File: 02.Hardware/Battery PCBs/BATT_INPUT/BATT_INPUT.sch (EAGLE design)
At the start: 39 parts, among them J1 70AAJ-4-M0, J4 DX07S016JA1R1500, U1 AT24C16D-STUM-T, U5 BQ24075, U9 Value

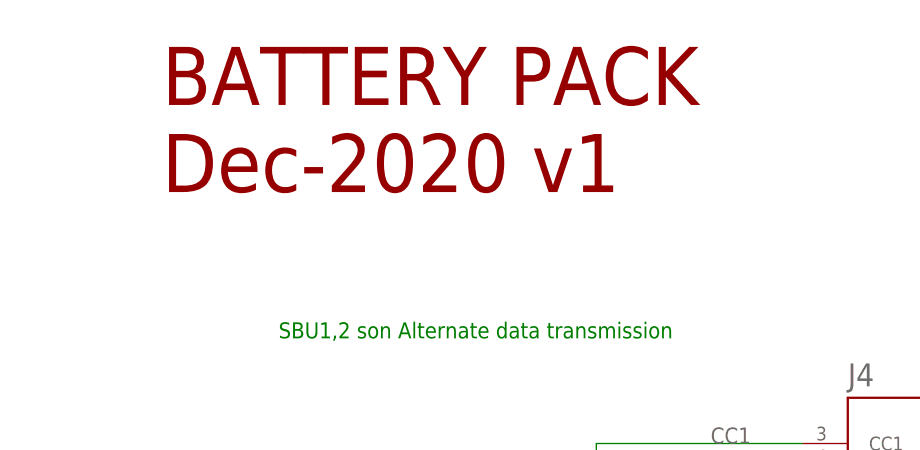
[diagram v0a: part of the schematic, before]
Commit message: Reorganizacion de directorios
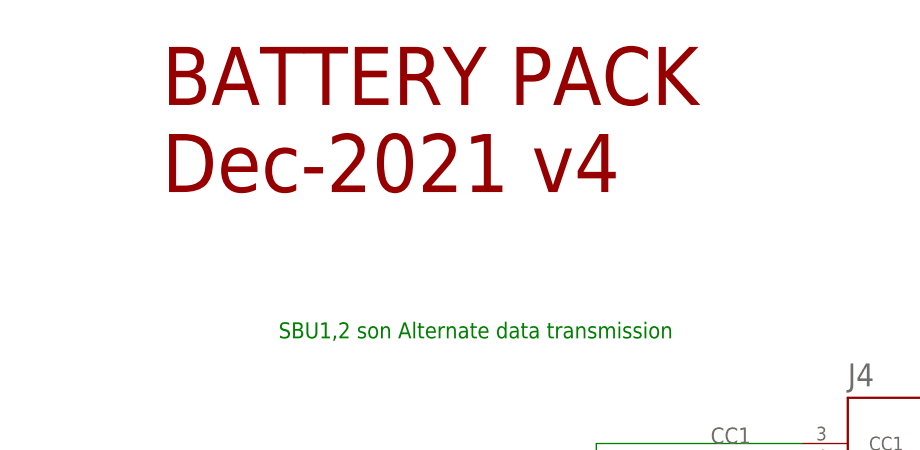
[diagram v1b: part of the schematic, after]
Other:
- note added: "BATTERY PACK Dec-2021 v4"
- note removed: "BATTERY PACK Dec-2020 v1"
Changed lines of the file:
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@@
 <plain>
 <text x="243.84" y="271.78" size="6.4516" layer="94">BATTERY PACK
-Dec-2020 v1</text>
+Dec-2021 v4 </text>
 <text x="331.216" y="51.308" size="1.27" layer="97" font="vector" align="top-left">Sets fast charge current
 - R_ISET range: 590-8.9k

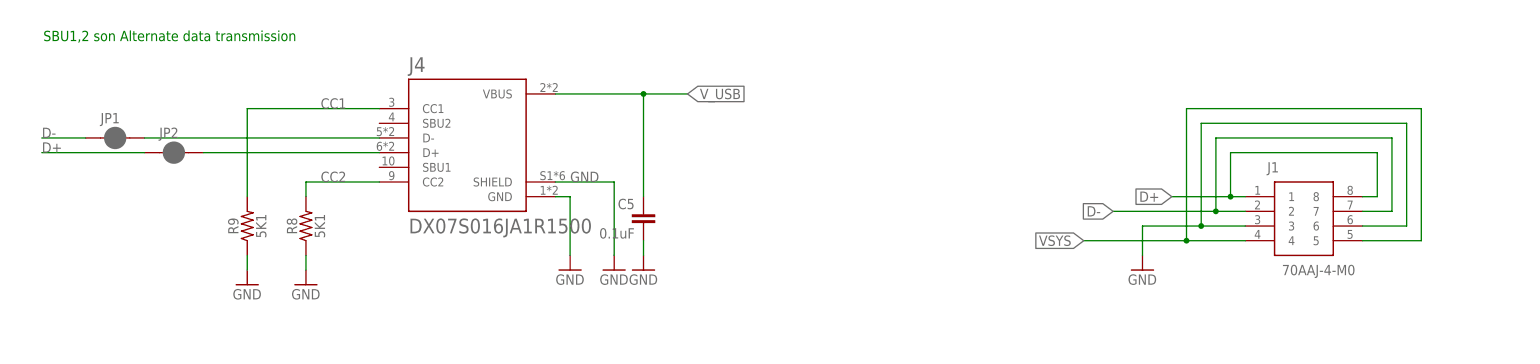
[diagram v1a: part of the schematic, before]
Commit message: Cambios revisados con David
Revision de los pcbs de la bateria.

En el DCDC se añade un diode Clamp (bat54s) en la medicion de la tension de salida.
Actualizacion de la BOM a v8.
Documentos de Cambios de versiones
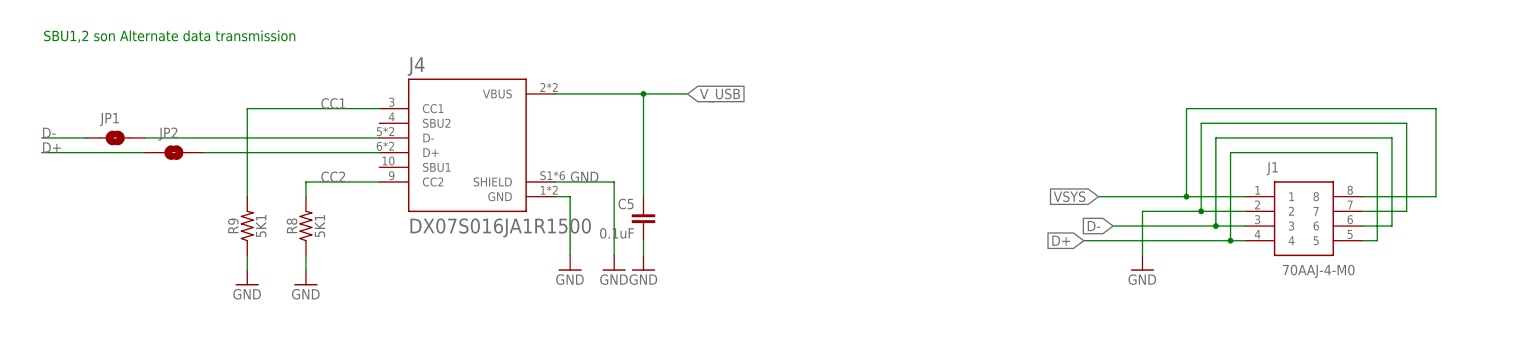
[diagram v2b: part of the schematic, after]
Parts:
- JP1, JP2: value JUMPER-SMT_2_NC_PASTE_SILK -> JUMPER-SMT_2_NO_SILK; device SparkFun-Jumpers:JUMPER-SMT_2_NC_PASTE_SILK -> SparkFun-Jumpers:JUMPER-SMT_2_NO_SILK
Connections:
- net D+: now also J1.4, J1.5; no longer J1.1, J1.8
- net D-: now also J1.3, J1.6; no longer J1.2, J1.7
- net GND: now also J1.2, J1.7; no longer J1.3, J1.6
- net VSYS: now also J1.1, J1.8; no longer J1.4, J1.5
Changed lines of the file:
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@@
 <part name="GND4" library="SparkFun-PowerSymbols" deviceset="GND" device=""/>
 <part name="GND9" library="SparkFun-PowerSymbols" deviceset="GND" device=""/>
-<part name="JP1" library="SparkFun-Jumpers" library_urn="urn:adsk.eagle:library:528" deviceset="JUMPER-SMT_2_NC_PASTE" device="_SILK" package3d_urn="urn:adsk.eagle:package:39282/1"/>
-<part name="JP2" library="SparkFun-Jumpers" library_urn="urn:adsk.eagle:library:528" deviceset="JUMPER-SMT_2_NC_PASTE" device="_SILK" package3d_urn="urn:adsk.eagle:package:39282/1"/>
+<part name="JP1" library="SparkFun-Jumpers" library_urn="urn:adsk.eagle:library:528" deviceset="JUMPER-SMT_2_NO" device="_SILK" package3d_urn="urn:adsk.eagle:package:39279/1"/>
+<part name="JP2" library="SparkFun-Jumpers" library_urn="urn:adsk.eagle:library:528" deviceset="JUMPER-SMT_2_NO" device="_SILK" package3d_urn="urn:adsk.eagle:package:39279/1"/>
 <part name="GND10" library="SparkFun-Aesthetics" deviceset="GND" device=""/>
 <part name="GND13" library="SparkFun-PowerSymbols" deviceset="GND" device=""/>
@@
 </segment>
 <segment>
-<pinref part="J1" gate="G$1" pin="3"/>
-<wire x1="464.82" y1="223.52" x2="457.2" y2="223.52" width="0.1524" layer="91"/>
-<pinref part="J1" gate="G$1" pin="6"/>
-<wire x1="457.2" y1="223.52" x2="447.04" y2="223.52" width="0.1524" layer="91"/>
-<wire x1="485.14" y1="223.52" x2="492.76" y2="223.52" width="0.1524" layer="91"/>
-<wire x1="492.76" y1="223.52" x2="492.76" y2="241.3" width="0.1524" layer="91"/>
+<wire x1="457.2" y1="226.06" x2="447.04" y2="226.06" width="0.1524" layer="91"/>
+<wire x1="492.76" y1="226.06" x2="492.76" y2="241.3" width="0.1524" layer="91"/>
 <wire x1="492.76" y1="241.3" x2="457.2" y2="241.3" width="0.1524" layer="91"/>
-<wire x1="457.2" y1="241.3" x2="457.2" y2="223.52" width="0.1524" layer="91"/>
-<junction x="457.2" y="223.52"/>
+<wire x1="457.2" y1="241.3" x2="457.2" y2="226.06" width="0.1524" layer="91"/>
 <pinref part="GND3" gate="1" pin="GND"/>
-<wire x1="447.04" y1="218.44" x2="447.04" y2="223.52" width="0.1524" layer="91"/>
+<wire x1="447.04" y1="218.44" x2="447.04" y2="226.06" width="0.1524" layer="91"/>
+<pinref part="J1" gate="G$1" pin="7"/>
+<wire x1="492.76" y1="226.06" x2="485.14" y2="226.06" width="0.1524" layer="91"/>
+<pinref part="J1" gate="G$1" pin="2"/>
+<wire x1="457.2" y1="226.06" x2="464.82" y2="226.06" width="0.1524" layer="91"/>
+<junction x="457.2" y="226.06"/>
 </segment>
 <segment>
@@
 </segment>
 <segment>
-<pinref part="J1" gate="G$1" pin="4"/>
-<wire x1="464.82" y1="220.98" x2="454.66" y2="220.98" width="0.1524" layer="91"/>
-<pinref part="J1" gate="G$1" pin="5"/>
-<wire x1="454.66" y1="220.98" x2="436.88" y2="220.98" width="0.1524" layer="91"/>
-<wire x1="485.14" y1="220.98" x2="495.3" y2="220.98" width="0.1524" layer="91"/>
-<wire x1="495.3" y1="220.98" x2="495.3" y2="243.84" width="0.1524" layer="91"/>
-<wire x1="495.3" y1="243.84" x2="454.66" y2="243.84" width="0.1524" layer="91"/>
-<wire x1="454.66" y1="243.84" x2="454.66" y2="220.98" width="0.1524" layer="91"/>
-<junction x="454.66" y="220.98"/>
-<label x="436.88" y="220.98" size="1.778" layer="95" rot="R180" xref="yes"/>
+<wire x1="454.66" y1="228.6" x2="439.42" y2="228.6" width="0.1524" layer="91"/>
+<wire x1="497.84" y1="228.6" x2="497.84" y2="243.84" width="0.1524" layer="91"/>
+<wire x1="497.84" y1="243.84" x2="454.66" y2="243.84" width="0.1524" layer="91"/>
+<wire x1="454.66" y1="243.84" x2="454.66" y2="228.6" width="0.1524" layer="91"/>
+<label x="439.42" y="228.6" size="1.778" layer="95" rot="R180" xref="yes"/>
+<pinref part="J1" gate="G$1" pin="1"/>
+<wire x1="454.66" y1="228.6" x2="464.82" y2="228.6" width="0.1524" layer="91"/>
+<junction x="454.66" y="228.6"/>
+<pinref part="J1" gate="G$1" pin="8"/>
+<wire x1="485.14" y1="228.6" x2="497.84" y2="228.6" width="0.1524" layer="91"/>
 </segment>
 <segment>
@@
 <net name="D-" class="0">
 <segment>
-<pinref part="J1" gate="G$1" pin="2"/>
-<wire x1="464.82" y1="226.06" x2="459.74" y2="226.06" width="0.1524" layer="91"/>
-<pinref part="J1" gate="G$1" pin="7"/>
-<wire x1="459.74" y1="226.06" x2="441.96" y2="226.06" width="0.1524" layer="91"/>
-<wire x1="485.14" y1="226.06" x2="490.22" y2="226.06" width="0.1524" layer="91"/>
-<wire x1="490.22" y1="226.06" x2="490.22" y2="238.76" width="0.1524" layer="91"/>
+<wire x1="459.74" y1="223.52" x2="441.96" y2="223.52" width="0.1524" layer="91"/>
+<wire x1="490.22" y1="223.52" x2="490.22" y2="238.76" width="0.1524" layer="91"/>
 <wire x1="490.22" y1="238.76" x2="459.74" y2="238.76" width="0.1524" layer="91"/>
-<wire x1="459.74" y1="238.76" x2="459.74" y2="226.06" width="0.1524" layer="91"/>
-<junction x="459.74" y="226.06"/>
-<label x="441.96" y="226.06" size="1.778" layer="95" rot="R180" xref="yes"/>
+<wire x1="459.74" y1="238.76" x2="459.74" y2="223.52" width="0.1524" layer="91"/>
+<label x="441.96" y="223.52" size="1.778" layer="95" rot="R180" xref="yes"/>
+<pinref part="J1" gate="G$1" pin="6"/>
+<wire x1="490.22" y1="223.52" x2="485.14" y2="223.52" width="0.1524" layer="91"/>
+<pinref part="J1" gate="G$1" pin="3"/>
+<wire x1="459.74" y1="223.52" x2="464.82" y2="223.52" width="0.1524" layer="91"/>
+<junction x="459.74" y="223.52"/>
 </segment>
 <segment>
@@
 <net name="D+" class="0">
 <segment>
-<pinref part="J1" gate="G$1" pin="1"/>
-<wire x1="464.82" y1="228.6" x2="462.28" y2="228.6" width="0.1524" layer="91"/>
-<wire x1="462.28" y1="228.6" x2="452.12" y2="228.6" width="0.1524" layer="91"/>
-<wire x1="462.28" y1="228.6" x2="462.28" y2="236.22" width="0.1524" layer="91"/>
-<junction x="462.28" y="228.6"/>
+<wire x1="462.28" y1="220.98" x2="436.88" y2="220.98" width="0.1524" layer="91"/>
+<wire x1="462.28" y1="220.98" x2="462.28" y2="236.22" width="0.1524" layer="91"/>
 <wire x1="462.28" y1="236.22" x2="487.68" y2="236.22" width="0.1524" layer="91"/>
-<wire x1="487.68" y1="236.22" x2="487.68" y2="228.6" width="0.1524" layer="91"/>
-<pinref part="J1" gate="G$1" pin="8"/>
-<wire x1="487.68" y1="228.6" x2="485.14" y2="228.6" width="0.1524" layer="91"/>
-<label x="452.12" y="228.6" size="1.778" layer="95" rot="R180" xref="yes"/>
-</segment>
-<segment>
+<label x="436.88" y="220.98" size="1.778" layer="95" rot="R180" xref="yes"/>
+<pinref part="J1" gate="G$1" pin="4"/>
+<wire x1="462.28" y1="220.98" x2="464.82" y2="220.98" width="0.1524" layer="91"/>
+<junction x="462.28" y="220.98"/>
+<pinref part="J1" gate="G$1" pin="5"/>
+<wire x1="487.68" y1="236.22" x2="487.68" y2="220.98" width="0.1524" layer="91"/>
+<wire x1="487.68" y1="220.98" x2="485.14" y2="220.98" width="0.1524" layer="91"/>
+</segment>
+<segment>

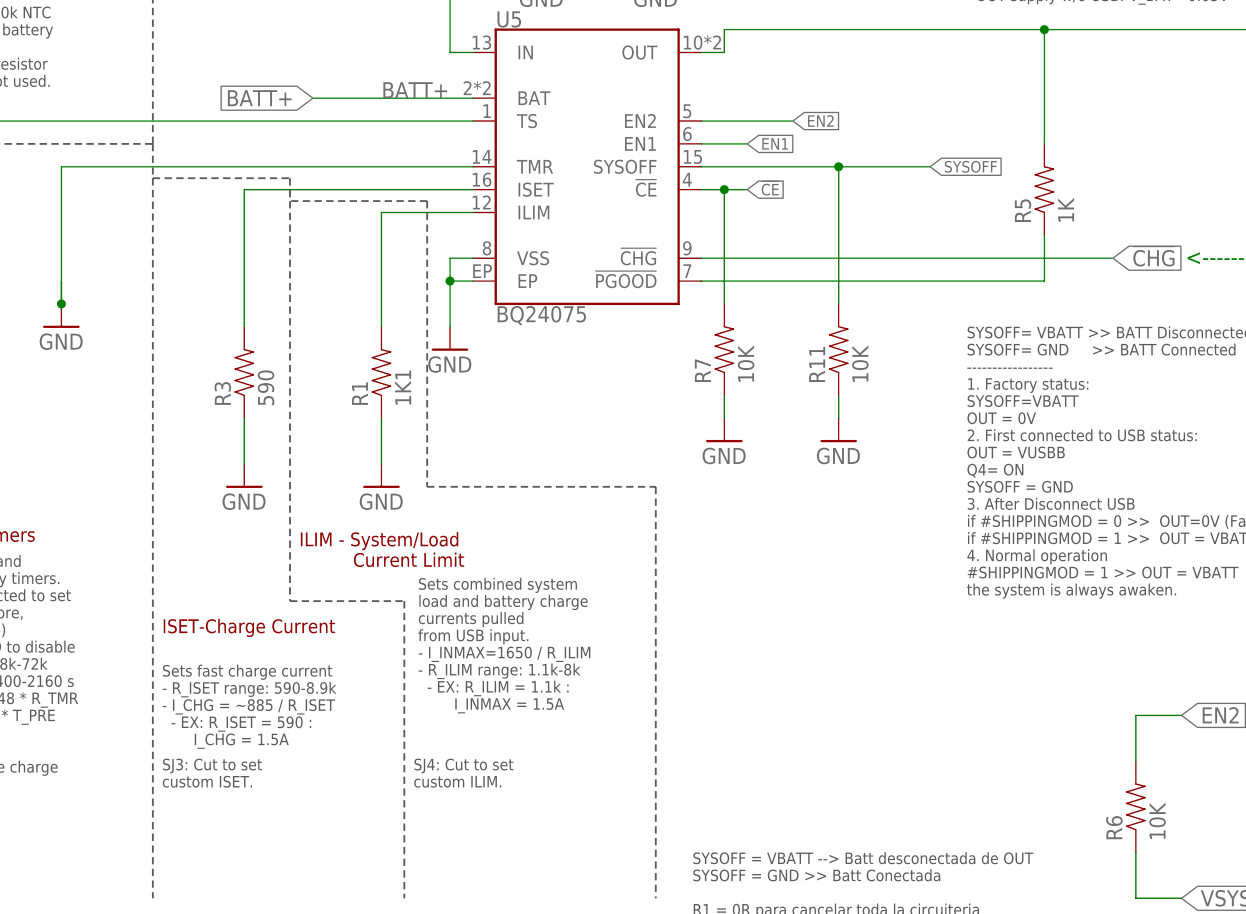
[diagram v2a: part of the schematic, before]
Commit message: Review general antes de produccion
Se modifica:
R13 --> El sensado de vosense estaba tarado para 3.3v en vez de 3v de vsupply
R15 --> Se baja el valor porque  no hace falta que sea tan alta
C10 --> Error de valor 470n en vez de 47n
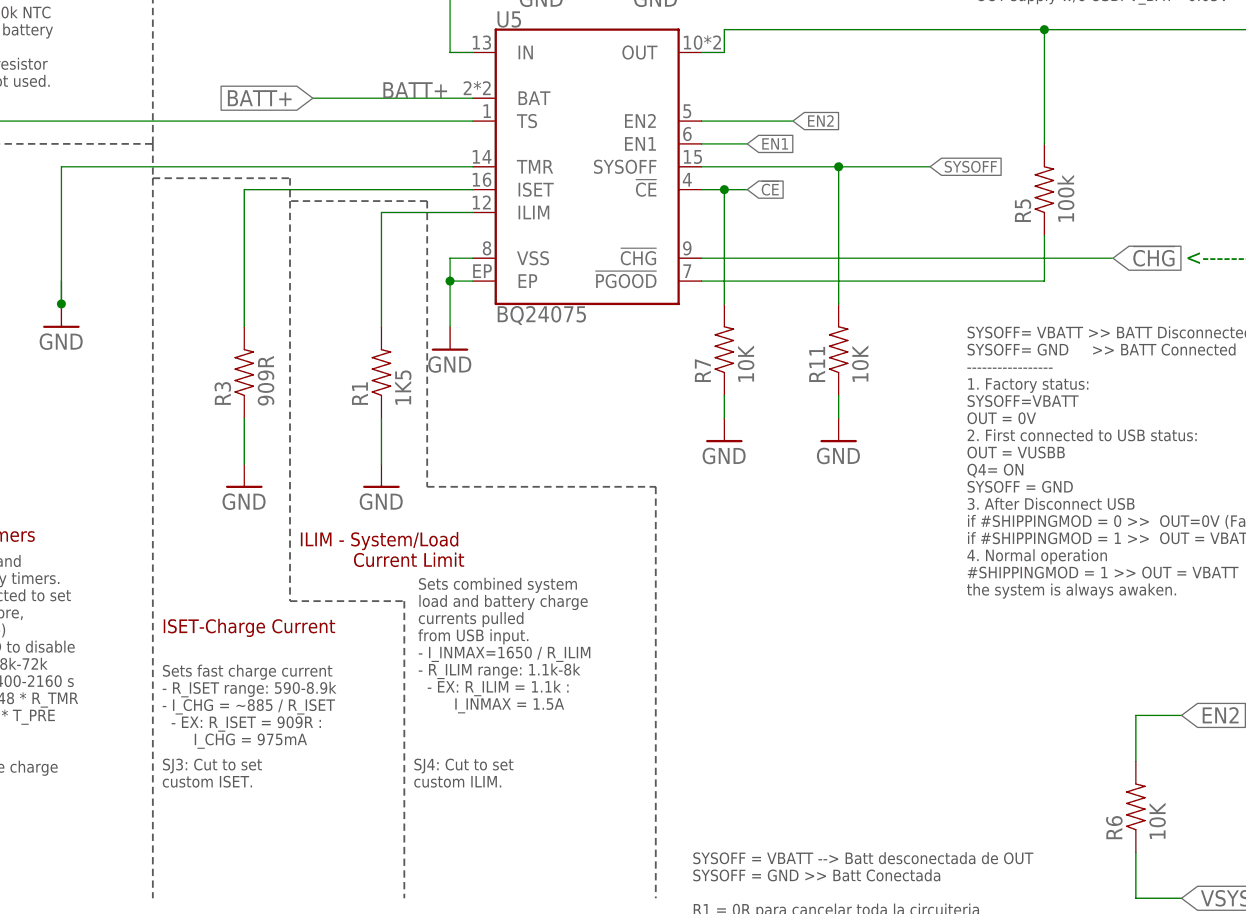
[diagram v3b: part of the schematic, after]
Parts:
- R1: value 1K1 -> 1K5
- R3: value 590 -> 909R
- R5: value 1K -> 100k
- U9: value Value -> BQ29700DSER
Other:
- note added: "Sets fast charge current - R_ISET range: 590-8.9k - I_CHG = ~885 / R_ISET - EX: R_ISET = 909R : I_CHG = 975mA"
- note removed: "Sets fast charge current - R_ISET range: 590-8.9k - I_CHG = ~885 / R_ISET - EX: R_ISET = 590 : I_CHG = 1.5A"
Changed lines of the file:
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@@
 <part name="C23" library="SparkFun-Capacitors" library_urn="urn:adsk.eagle:library:510" deviceset="10UF10V10%(0805)" device="" value="10uF / 10V"/>
 <part name="GND53" library="SparkFun" deviceset="GND" device=""/>
-<part name="U9" library="BQ2970" deviceset="BQ29700DSER" device="" value="Value"/>
+<part name="U9" library="BQ2970" deviceset="BQ29700DSER" device="" value="BQ29700DSER"/>
 <part name="+RAWBATT+" library="wirepad" library_urn="urn:adsk.eagle:library:412" deviceset="SMD5" device="" package3d_urn="urn:adsk.eagle:package:30841/1"/>
 <part name="-RAWBATT-" library="wirepad" library_urn="urn:adsk.eagle:library:412" deviceset="SMD5" device="" package3d_urn="urn:adsk.eagle:package:30841/1"/>
@@
 <part name="R7" library="SparkFun-Resistors" deviceset="RESISTOR" device="0402" value="10K"/>
 <part name="R11" library="SparkFun-Resistors" deviceset="RESISTOR" device="0402" value="10K"/>
-<part name="R1" library="SparkFun-Resistors" deviceset="RESISTOR" device="0402" value="1K1"/>
-<part name="R3" library="SparkFun-Resistors" deviceset="RESISTOR" device="0402" value="590"/>
+<part name="R1" library="SparkFun-Resistors" deviceset="RESISTOR" device="0402" value="1K5"/>
+<part name="R3" library="SparkFun-Resistors" deviceset="RESISTOR" device="0402" value="909R"/>
 <part name="R17" library="SparkFun-Resistors" deviceset="RESISTOR" device="0402" value="10K"/>
 <part name="C1" library="SparkFun-Capacitors" deviceset="1.0UF" device="-0603-16V-10%" value="1.0uF"/>
@@
 <part name="R12" library="SparkFun-Resistors" deviceset="RESISTOR" device="0402" value="10K"/>
 <part name="GND2" library="SparkFun-Aesthetics" deviceset="GND" device=""/>
-<part name="R5" library="SparkFun-Resistors" deviceset="RESISTOR" device="0402" value="1K"/>
+<part name="R5" library="SparkFun-Resistors" deviceset="RESISTOR" device="0402" value="100k"/>
 <part name="R6" library="SparkFun-Resistors" deviceset="RESISTOR" device="0402" value="10K"/>
 <part name="J1" library="ANTENNA" deviceset="70AAJ-4-M0" device=""/>
@@
 - R_ISET range: 590-8.9k
 - I_CHG = ~885 / R_ISET
-  - EX: R_ISET = 590 :
-       I_CHG = 1.5A</text>
+  - EX: R_ISET = 909R :
+       I_CHG = 975mA</text>
 <text x="359.664" y="60.96" size="1.27" layer="97" font="vector" align="top-left">Sets combined system
 load and battery charge
